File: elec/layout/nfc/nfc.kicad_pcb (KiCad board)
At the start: 2 copper layers, 27 parts, among them U1 _NXP_Semicon_PN5321A3HN_C106_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

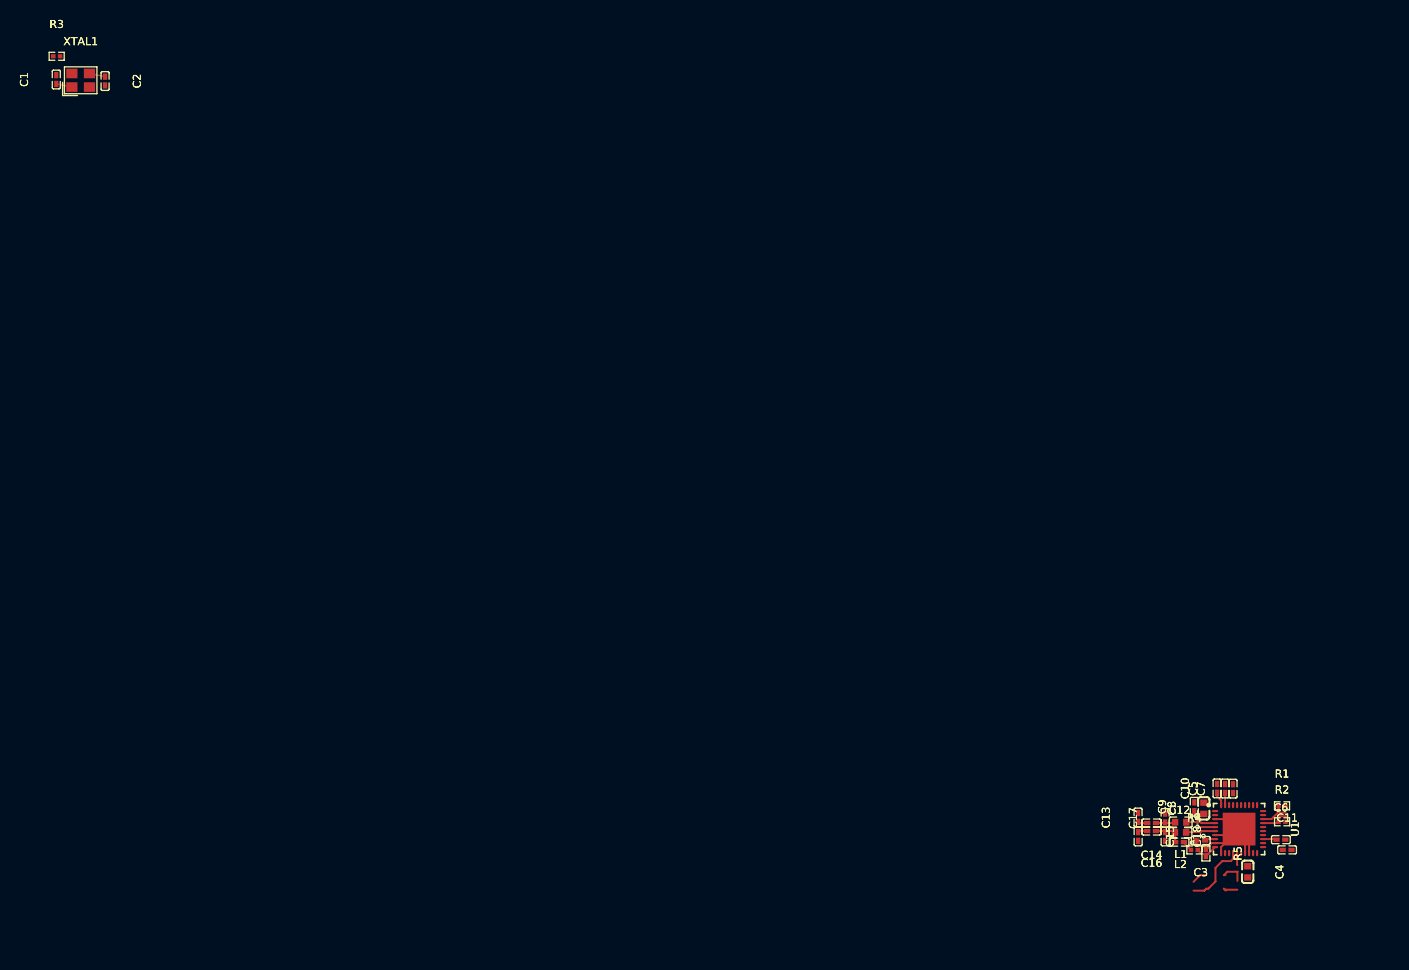
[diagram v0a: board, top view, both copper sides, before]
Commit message: kinda fix amp layout
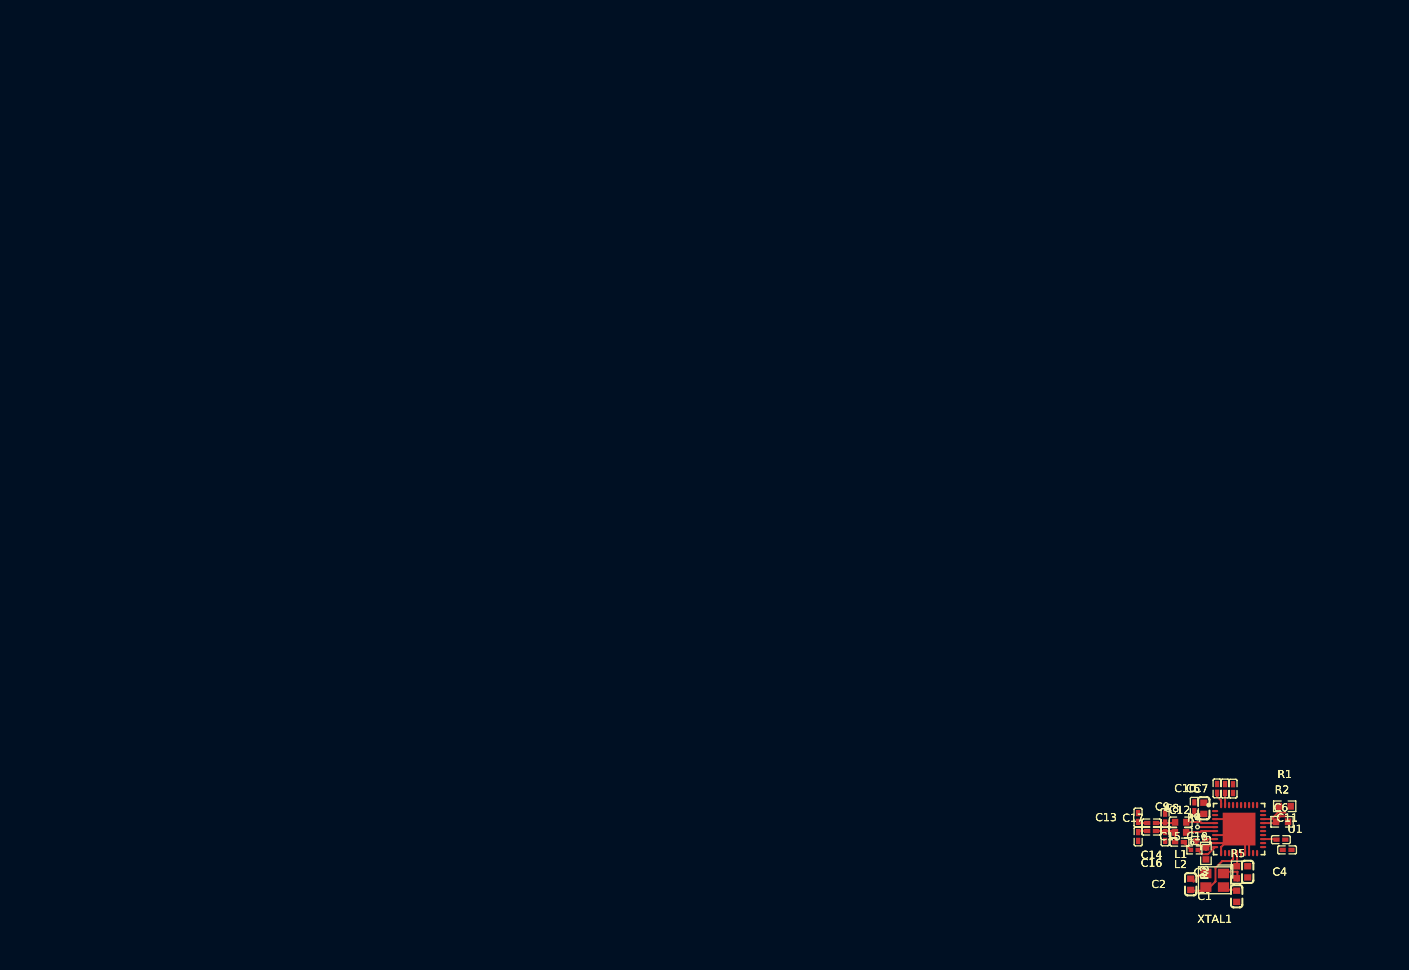
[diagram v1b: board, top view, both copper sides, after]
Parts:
- C1, C2: value 20pF ±5% 50V C0G -> 100nF ±10% 50V X7R; footprint lcsc:C0402 -> atopile:C0603-bd72f6
- C10, C11, C12, C13, C15, C17, C18, C3, C5, C6, C7, C9: footprint lcsc:C0402 -> atopile:C0402-b3ef17
- C14, C16: value 20pF ±5% 50V C0G -> 22pF ±5% 50V C0G; footprint lcsc:C0402 -> atopile:C0402-b3ef17
- C4, C8: footprint lcsc:C0603 -> atopile:C0603-bd72f6
- L1, L2: value 560nH ±5% 450mA 480mΩ -> (none); footprint lcsc:IND-SMD_L1.6-W0.8-1 -> atopile:IND-SMD_L1.6-W0.8-1-cea827
- R1, R2, R3, R5: value 5.1kΩ ±1% 62.5mW -> 10kΩ ±1% 100mW; footprint lcsc:R0402 -> atopile:R0603-ebcab9
- R4: footprint lcsc:R0402 -> atopile:R0402-56259e
- U1: value _NXP_Semicon_PN5321A3HN_C106_51 -> (none); footprint lcsc:QFN-40_L6.0-W6.0-P0.50-BL-EP4.1 -> atopile:QFN-40_L6.0-W6.0-P0.50-BL-EP4.1-54a13c
- XTAL1: value Crystal -> (none); footprint lcsc:CRYSTAL-SMD_4P-L3.2-W2.5-BL -> atopile:CRYSTAL-SMD_4P-L3.2-W2.5-BL-e199c8
- moved C1 179.4 mm to (144.5, 102.0)
- moved R3 179.3 mm to (144.5, 99.0), turned to 90 degrees
- moved XTAL1 173.5 mm to (141.8, 100.0), turned to 180 degrees
- moved C2 168.8 mm to (138.8, 100.5), turned to 90 degrees
- moved R1 0.34 mm to (150.5, 90.8)
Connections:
- net aux1 renamed AUX1
- net aux2 renamed AUX2
- net loadmod renamed LOADMOD
- net miso_p71 renamed MISO_P71
- net net-10 renamed MOSI_SDA_HSU_TX
- net net-11 renamed OSCOUT
- net net-12 renamed line
- net net-2 renamed TX1
- net net-4 renamed RX
- net net-5 renamed SVDD
- net net-6 renamed hv-1
- net net-7 renamed NSS_P50_SCL_HSU_RX
- net net-8 renamed TX2
- net net-9 renamed OSCIN
- net oscillator-net renamed unnamed[0]
- net p30_uart_rx renamed P30_UART_RX
- net p31_uart_tx renamed P31_UART_TX
- net p32_int0 renamed P32_INT0
- net p33_int1 renamed P33_INT1
- net p34_sic_clk renamed P34_SIC_CLK
- net p70_irq renamed P70_IRQ
- net power_vmid-lv renamed gnd
- net rstpd_n renamed RSTPD_N
- net sck_p72 renamed SCK_P72
- net sigin renamed SIGIN
- net signal renamed RSTOUT_N
- net sigout renamed SIGOUT
- C1 pad 2: net-1 -> gnd-1
- C10 pad 2: net-1 -> gnd-1
- C11 pad 1: net-1 -> gnd-1
- C12 pad 2: net-3 -> net
- C13 pad 1: net -> line-1
- C13 pad 2: net-1 -> gnd-1
- C14 pad 2: net -> line-1
- C15 pad 2: net-1 -> gnd-1
- C17 pad 2: net-1 -> gnd-1
- C18 pad 2: net-1 -> gnd-1
- C2 pad 2: net-1 -> gnd-1
- C3 pad 2: net-1 -> gnd-1
- C4 pad 2: net-1 -> gnd-1
- C5 pad 2: net-1 -> gnd-1
- C6 pad 2: net-1 -> gnd-1
- C7 pad 2: power_svdd-lv -> gnd-1
- C8 pad 2: net-1 -> gnd-1
- C9 pad 2: net-1 -> gnd-1
- R4 pad 1: net-3 -> net
- R5 pad 1: net-1 -> gnd-1
- U1 pad 1: net-1 -> gnd-1
- U1 pad 11: net-1 -> gnd-1
- U1 pad 17: net-1 -> gnd-1
- U1 pad 18: net-1 -> gnd-1
- U1 pad 19: p35 -> nfc_ic-net
- U1 pad 20: nfc_ic-net -> nfc_ic.footprint.pins[12].net-net
- U1 pad 21: nfc_ic-net -> nfc_ic.footprint.pins[13].net-net
- U1 pad 22: nfc_ic-net -> nfc_ic.footprint.pins[14].net-net
- U1 pad 3: net-1 -> gnd-1
- U1 pad 41: net-1 -> gnd-1
- U1 pad 7: net-1 -> gnd-1
- U1 pad 9: net-1 -> gnd-1
- XTAL1 pad 2: net-1 -> gnd-1
- XTAL1 pad 4: net-1 -> gnd-1
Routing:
- net gnd-1: track 0.00 -> 29.9 mm, vias 0 -> 1
- net net-1: track 25.8 -> 0.00 mm, vias 1 -> 0
- net MOSI_SDA_HSU_TX: track 4.67 -> 0.00 mm
- net (no net): track 0.00 -> 4.67 mm
- net TX1: track 8.00 -> 3.96 mm
- net unnamed[0]: track 5.21 -> 3.22 mm
- net OSCIN: track 10.3 -> 8.31 mm
- net net-3: track 1.57 -> 0.00 mm
- net line-1: track 0.00 -> 1.20 mm

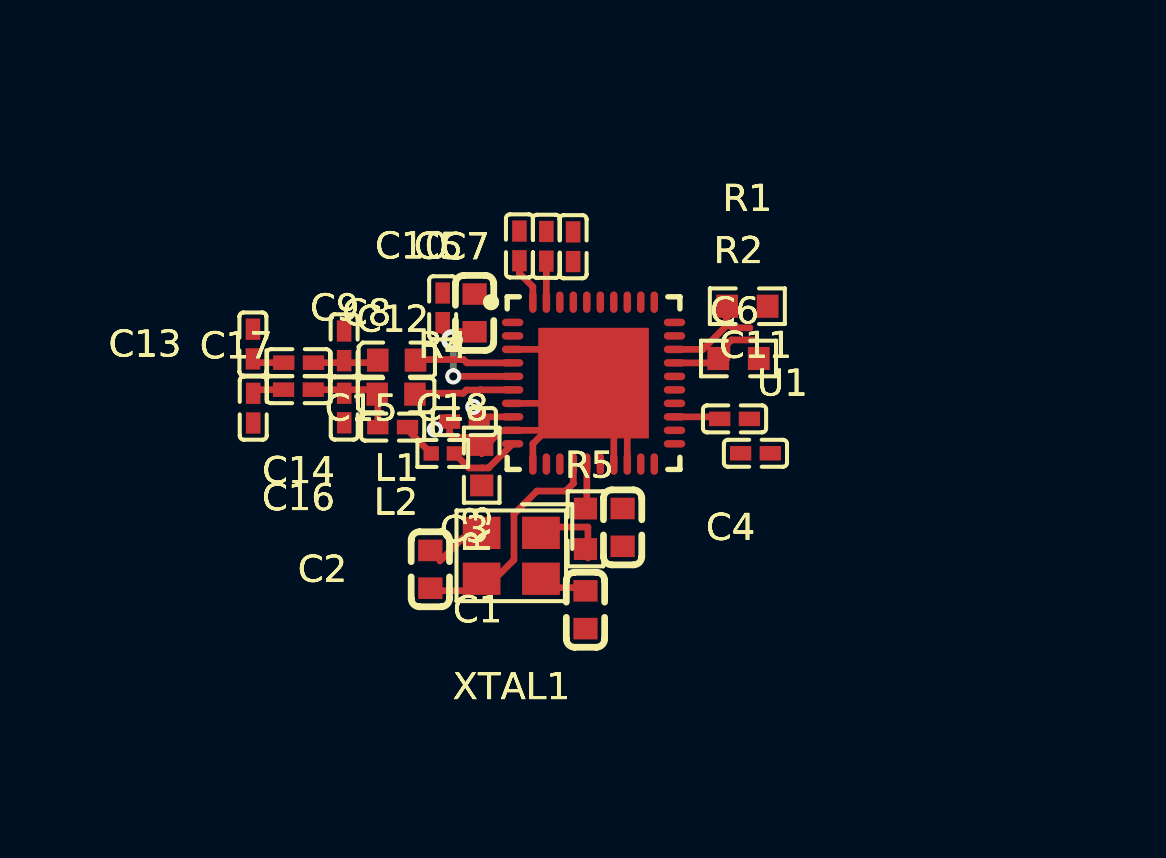
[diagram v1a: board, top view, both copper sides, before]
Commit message: Fix: NFC layout
- fix packages
- fix vmid short
- fix unconnected nets
- fix linking issues
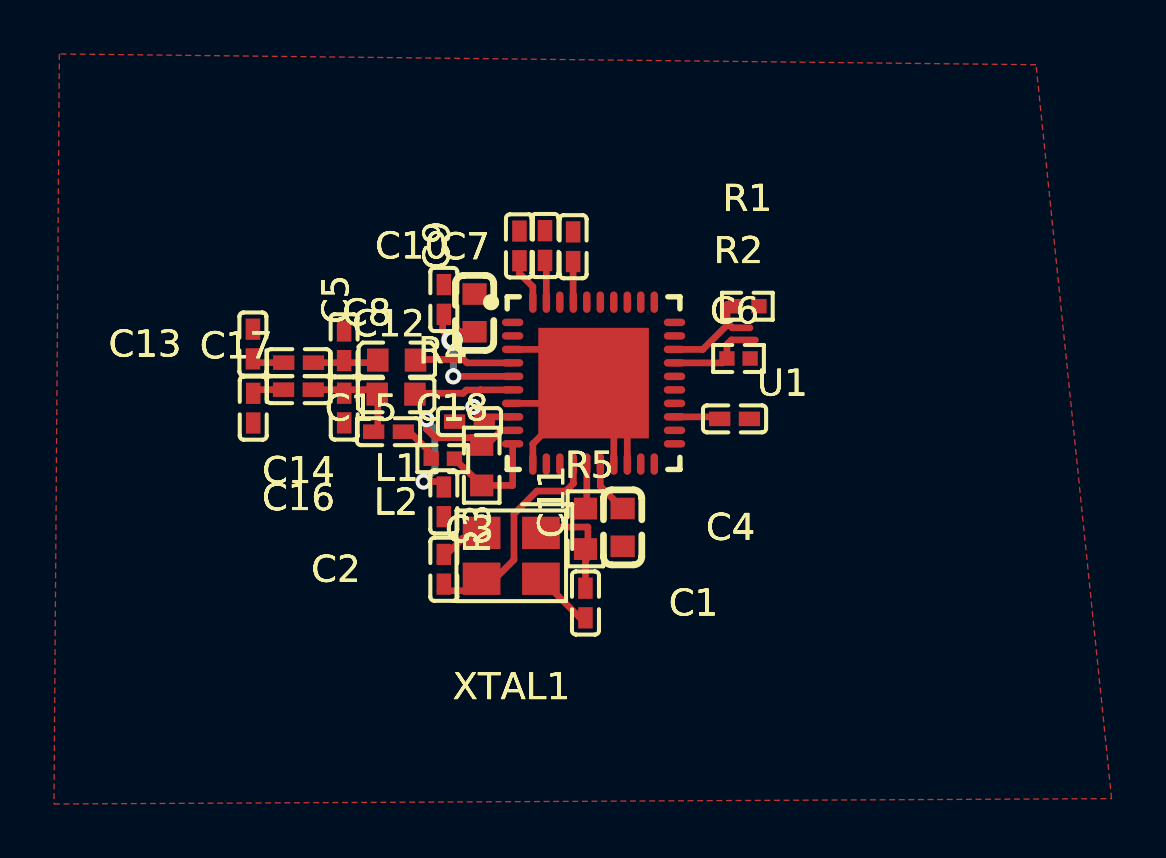
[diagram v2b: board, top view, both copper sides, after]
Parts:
- C1, C2: value 100nF ±10% 50V X7R -> 100nF ±10% 16V X7R; footprint atopile:C0603-bd72f6 -> atopile:C0402-b3ef17
- R1, R2: value 10kΩ ±1% 100mW -> 100kΩ ±1% 62.5mW; footprint atopile:R0603-ebcab9 -> atopile:R0402-56259e
- moved C11 11.7 mm to (139.2, 98.0), turned to -90 degrees
- moved C9 4.44 mm to (143.0, 88.5)
- moved C5 4.28 mm to (139.2, 90.5)
- moved C2 0.50 mm to (139.2, 100.5)
- moved C1 0.25 mm to (144.5, 101.8), turned to -90 degrees
- moved C12 0.23 mm to (137.2, 95.4)
- moved R4 0.19 mm to (139.2, 96.4)
- moved C3 0.19 mm to (140.2, 95.0)
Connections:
- net unnamed[0] renamed oscillator-net
- C1 pad 2: gnd-1 -> gnd
- C10 pad 1: hv-1 -> hv
- C10 pad 2: gnd-1 -> gnd
- C11 pad 1: gnd-1 -> VMID
- C13 pad 1: line-1 -> line
- C13 pad 2: gnd-1 -> gnd
- C14 pad 2: line-1 -> line
- C15 pad 1: line -> line-1
- C15 pad 2: gnd-1 -> gnd
- C16 pad 2: line -> line-1
- C17 pad 2: gnd-1 -> gnd
- C18 pad 2: gnd-1 -> gnd
- C2 pad 2: gnd-1 -> gnd
- C3 pad 1: hv-1 -> hv
- C3 pad 2: gnd-1 -> gnd
- C4 pad 1: hv-1 -> hv
- C4 pad 2: gnd-1 -> gnd
- C5 pad 1: hv-1 -> hv
- C5 pad 2: gnd-1 -> gnd
- C6 pad 1: hv-1 -> hv
- C6 pad 2: gnd-1 -> gnd
- C7 pad 2: gnd-1 -> gnd
- C8 pad 1: hv-1 -> hv
- C8 pad 2: gnd-1 -> gnd
- C9 pad 1: hv-1 -> hv
- C9 pad 2: gnd-1 -> gnd
- R1 pad 2: hv -> hv-1
- R2 pad 2: hv -> hv-1
- R5 pad 1: gnd-1 -> VMID
- U1 pad 1: gnd-1 -> gnd
- U1 pad 11: gnd-1 -> gnd
- U1 pad 16: hv-1 -> hv
- U1 pad 17: gnd-1 -> gnd
- U1 pad 18: gnd-1 -> gnd
- U1 pad 23: hv-1 -> hv
- U1 pad 3: gnd-1 -> gnd
- U1 pad 39: hv-1 -> hv
- U1 pad 40: hv-1 -> hv
- U1 pad 41: gnd-1 -> gnd
- U1 pad 5: hv-1 -> hv
- U1 pad 7: gnd-1 -> gnd
- U1 pad 8: hv-1 -> hv
- U1 pad 9: gnd-1 -> VMID
- XTAL1 pad 2: gnd-1 -> gnd
- XTAL1 pad 4: gnd-1 -> gnd
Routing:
- net gnd-1: track 29.9 -> 0.00 mm, vias 1 -> 0
- net gnd: track 0.00 -> 24.8 mm
- net hv: track 0.00 -> 14.3 mm, vias 0 -> 3
- net hv-1: track 12.3 -> 0.00 mm, vias 3 -> 0
- net VMID: track 0.00 -> 7.41 mm, vias 0 -> 2
- net MOSI_SDA_HSU_TX: track 0.00 -> 4.67 mm
- net (no net): track 4.67 -> 0.00 mm
- net SVDD: track 0.00 -> 1.51 mm
- net oscillator-net: track 3.22 -> 4.67 mm
- net RX: track 2.75 -> 4.11 mm
- added copper zone on F.Cu, net gnd

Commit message: remove pour
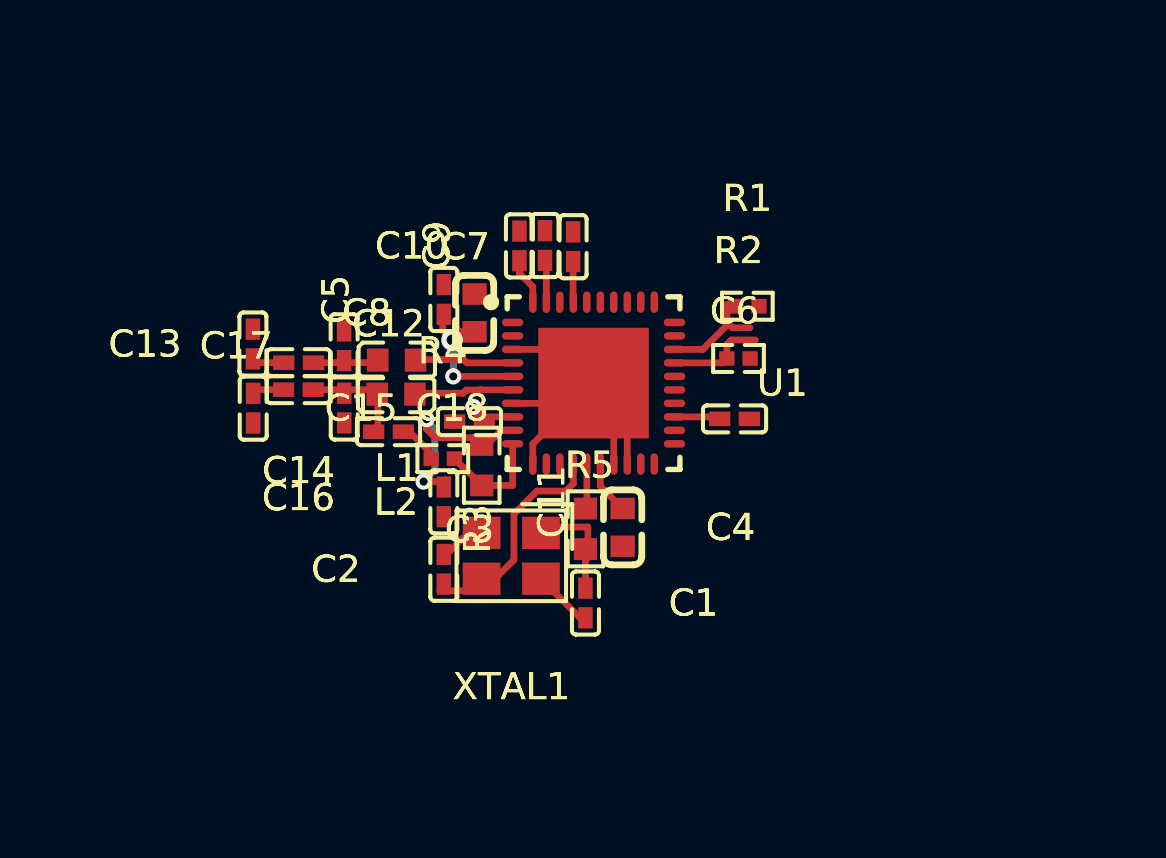
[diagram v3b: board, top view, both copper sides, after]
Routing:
- removed copper zone on F.Cu, net gnd
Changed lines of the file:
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@@
 		(net 37)
-	)
-	(zone
-		(net 37)
-		(net_name "gnd")
-		(layer "F.Cu")
-		(hatch edge 0.5)
-		(connect_pads
-			(clearance 0.5)
-		)
-		(min_thickness 0.25)
-		(filled_areas_thickness no)
-		(fill yes
-			(thermal_gap 0.5)
-			(thermal_bridge_width 0.5)
-		)
-		(polygon
-			(pts
-				(xy 125 81.4) (xy 124.8 109.2) (xy 164 109) (xy 161.2 81.8)
-			)
-		)
 	)
 	(embedded_fonts no)

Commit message: run ato
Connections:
- C13 pad 1: line -> line-1
- C14 pad 2: line -> line-1
- C15 pad 1: line-1 -> line
- C16 pad 2: line-1 -> line
